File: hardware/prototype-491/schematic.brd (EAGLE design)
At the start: 160 x 100 mm, 22 parts, among them IC1 LM2576T, IC2 LM2576T, Q1 220mA/50V/3.5Ω, Q2 220mA/50V/3.5Ω

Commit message: routed signals
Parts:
- added J2: (no value), SparkFun-Connectors:MOLEX-1X2
- moved J1 189.3 mm to (83.8, 96.5), turned to 180 degrees
- moved Q1 179.0 mm to (97.8, 12.7), turned to 270 degrees
- moved C4 161.8 mm to (92.7, 36.8), turned to 270 degrees
- moved R5 157.7 mm to (105.4, 40.6), turned to 270 degrees
- moved R4 151.0 mm to (105.4, 29.2), turned to 270 degrees
- moved C2 146.2 mm to (92.7, 54.6), turned to 180 degrees
- moved R3 145.1 mm to (105.4, 19.1), turned to 270 degrees
- moved JP8 144.6 mm to (67.3, 67.3)
- moved R2 140.4 mm to (105.4, 8.89), turned to 270 degrees
- moved IC2 134.7 mm to (77.5, 45.7), turned to 180 degrees
- moved MCU 131.7 mm to (5.08, 102.9), turned to 270 degrees
- moved D2 129.3 mm to (72.4, 7.62), turned to 180 degrees
- moved IC1 123.3 mm to (77.5, 16.5), turned to 180 degrees
- moved Q2 121.5 mm to (97.8, 25.4), turned to 90 degrees
- moved R1 112.5 mm to (36.8, 27.9), turned to 270 degrees
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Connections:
- net GND: now also J2.2
- net VCC: now also J2.1
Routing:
- net +5V: track 0.00 -> 220.4 mm
- net TX_3V3: track 0.00 -> 111.7 mm, vias 0 -> 1
- net 3.3V: track 0.00 -> 107.7 mm
- net TX_5V: track 0.00 -> 92.9 mm
- net RX_5V: track 0.00 -> 69.5 mm
- net SDA: track 0.00 -> 67.9 mm
- net SCL: track 0.00 -> 61.8 mm
- net N$4: track 0.00 -> 39.5 mm
- net N$1: track 0.00 -> 34.6 mm
- net VCC: track 0.00 -> 26.9 mm
- net N$9: track 0.00 -> 13.7 mm
- net RX_3V3: track 0.00 -> 10.0 mm
- added copper zone on layer 1, net GND
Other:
- board size 160 x 100 mm -> 116.8 x 110.2 mm
- board text added: "ADXL345 Board"
- board text added: "GND"
- board text added: "VS"

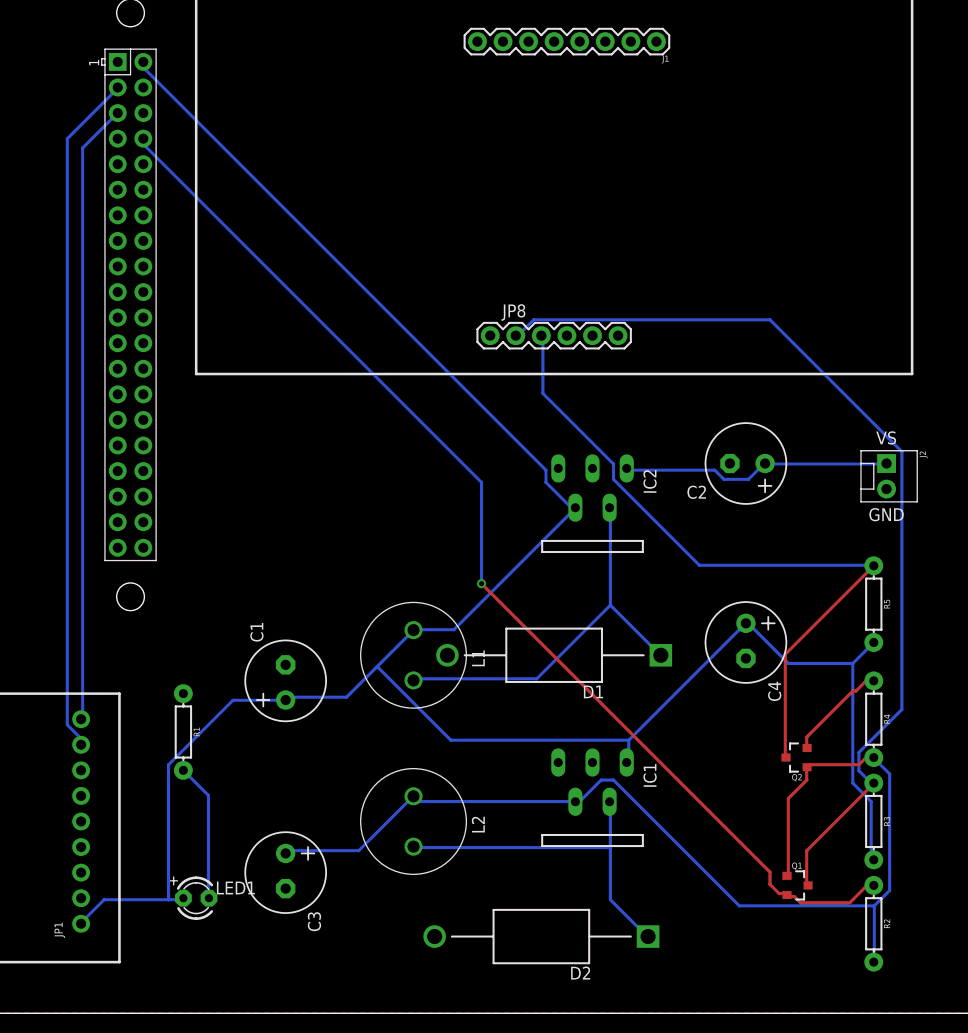
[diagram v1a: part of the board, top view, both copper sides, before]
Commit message: added status LEDs to main board, completed board for CAN test module
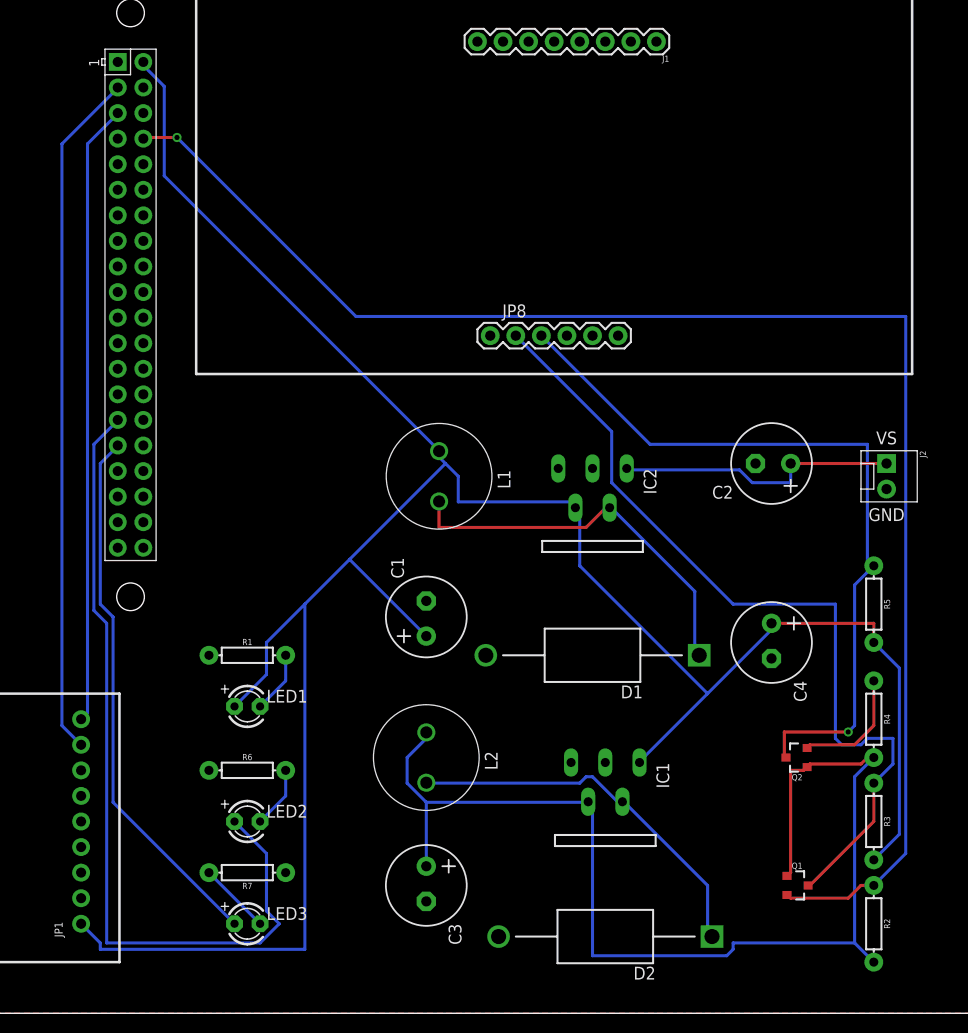
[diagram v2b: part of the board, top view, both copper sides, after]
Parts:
- added LED2, LED3: (no value), adafruit:LED3MM
- added R6, R7: 10k, SparkFun-Resistors:AXIAL-0.3
- moved LED1 19.7 mm to (43.2, 30.5)
- moved L1 18.0 mm to (62.2, 53.3)
- moved C1 15.3 mm to (61.0, 39.4)
- moved C3 14.0 mm to (61.0, 12.7)
- moved R1 9.92 mm to (43.2, 35.6), turned to 0 degrees
- moved L2 6.48 mm to (61.0, 25.4)
- moved D2 6.35 mm to (78.7, 7.62)
- moved D1 3.81 mm to (77.5, 35.6)
- moved C2 2.54 mm to (95.2, 54.6)
- moved C4 2.54 mm to (95.2, 36.8)
- moved IC1 1.27 mm to (78.7, 16.5)
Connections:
- new net N$2: LED2.A, MCU.29
- new net N$3: LED3.A, MCU.31
- new net N$5: LED2.K, R6.P$2
- new net N$6: LED3.K, R7.P$2
- net GND: now also R6.P$1, R7.P$1
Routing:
- net N$2: track 0.00 -> 83.4 mm
- net N$3: track 0.00 -> 53.7 mm
- net TX_3V3: track 111.7 -> 150.2 mm
- net +5V: track 220.4 -> 249.3 mm
- net TX_5V: track 92.9 -> 83.5 mm
- net N$9: track 13.7 -> 6.13 mm
- net N$6: track 0.00 -> 7.18 mm
- net 3.3V: track 107.7 -> 114.9 mm
- net RX_5V: track 69.5 -> 76.2 mm, vias 0 -> 1
- net N$5: track 0.00 -> 6.13 mm
- net N$1: track 34.6 -> 38.2 mm
- net RX_3V3: track 10.0 -> 12.0 mm
- net VCC: track 26.9 -> 28.3 mm

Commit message: CAM files for PCB
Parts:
- J1: value (none) -> OBD_CONN
- J2: value (none) -> SUPPLY
- JP1: value (none) -> ADXL345
- JP8: value DNP -> UART_CONN
- L1, L2: value (none) -> 100uH
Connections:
- removed net VCC: C2.+, IC2.1, J2.1
- net VBAT: now also C2.+, IC2.1, J2.1
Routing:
- net VBAT: track 0.00 -> 79.8 mm, vias 0 -> 1
- net TX_3V3: track 150.2 -> 116.0 mm
- net N$2: track 83.4 -> 49.9 mm
- net VCC: track 28.3 -> 0.00 mm
- net +5V: track 249.3 -> 234.0 mm, vias 0 -> 1
- net TX_5V: track 83.5 -> 93.2 mm
- net RX_5V: track 76.2 -> 69.7 mm, vias 1 -> 0
- net 3.3V: track 114.9 -> 108.7 mm
- net N$4: track 39.0 -> 36.5 mm
- net RX_3V3: track 12.0 -> 9.82 mm
- net N$3: track 53.7 -> 53.8 mm, vias 0 -> 1
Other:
- board text added: "ECE491Group7 Vehicle Immobilizer"

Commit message: all arduino / tester code
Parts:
- moved C1 41.2 mm to (95.2, 16.5), turned to 270 degrees
- moved Q1 5.08 mm to (97.8, 7.62)
- moved L1 4.58 mm to (59.7, 49.5), turned to 270 degrees
- moved L2 3.81 mm to (61.0, 29.2), turned to 270 degrees
- moved D1 2.54 mm to (77.5, 38.1)
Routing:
- net 3.3V: track 108.7 -> 126.9 mm, vias 0 -> 1
- net TX_5V: track 93.2 -> 79.8 mm
- net TX_3V3: track 116.0 -> 128.5 mm
- net N$1: track 38.2 -> 42.0 mm
- net +5V: track 234.0 -> 231.4 mm, vias 1 -> 0
- net VBAT: track 79.8 -> 81.4 mm, vias 1 -> 0
- net N$3: track 53.8 -> 54.5 mm
- net N$4: track 36.5 -> 37.1 mm

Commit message: test module updates
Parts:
- moved R2 74.0 mm to (44.5, 50.8), turned to 90 degrees
- moved R3 63.9 mm to (44.5, 38.1), turned to 90 degrees
- moved R5 55.5 mm to (50.8, 50.8), turned to 90 degrees
- moved R4 55.3 mm to (50.8, 38.1), turned to 90 degrees
- moved Q1 53.8 mm to (47.0, 25.4), turned to 0 degrees
- moved Q2 51.8 mm to (47.0, 15.2), turned to 0 degrees
- moved C3 44.7 mm to (97.8, 38.1), turned to 90 degrees
- moved L1 44.0 mm to (96.5, 25.4), turned to 0 degrees
- moved L2 40.3 mm to (96.5, 10.2), turned to 0 degrees
- moved C1 17.3 mm to (78.7, 21.6)
- moved R1 16.1 mm to (38.1, 50.8), turned to 270 degrees
- moved R6 14.9 mm to (38.1, 38.1), turned to 270 degrees
- moved D2 14.5 mm to (64.8, 11.4)
- moved IC1 13.3 mm to (66.0, 20.3)
- moved D1 11.4 mm to (66.0, 38.1)
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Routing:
- net TX_3V3: track 128.5 -> 64.1 mm, vias 1 -> 0
- net +5V: track 231.4 -> 192.0 mm
- net TX_5V: track 79.8 -> 57.6 mm
- net 3.3V: track 126.9 -> 148.0 mm, vias 1 -> 4
- net N$9: track 6.19 -> 23.4 mm, vias 0 -> 1
- net RX_3V3: track 9.81 -> 21.2 mm, vias 0 -> 1
- net N$5: track 6.12 -> 17.5 mm, vias 0 -> 1
- net N$2: track 49.7 -> 39.1 mm, vias 0 -> 1
- net N$4: track 37.1 -> 47.3 mm
- net VBAT: track 81.4 -> 71.3 mm
- net N$3: track 54.5 -> 45.3 mm
- net RX_5V: track 70.1 -> 61.1 mm, vias 0 -> 1
- net N$1: track 42.0 -> 35.9 mm
- net SCL: track 61.8 -> 59.0 mm
- net SDA: track 68.0 -> 65.4 mm
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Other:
- board size 116.8 x 110.2 mm -> 111.7 x 103.8 mm

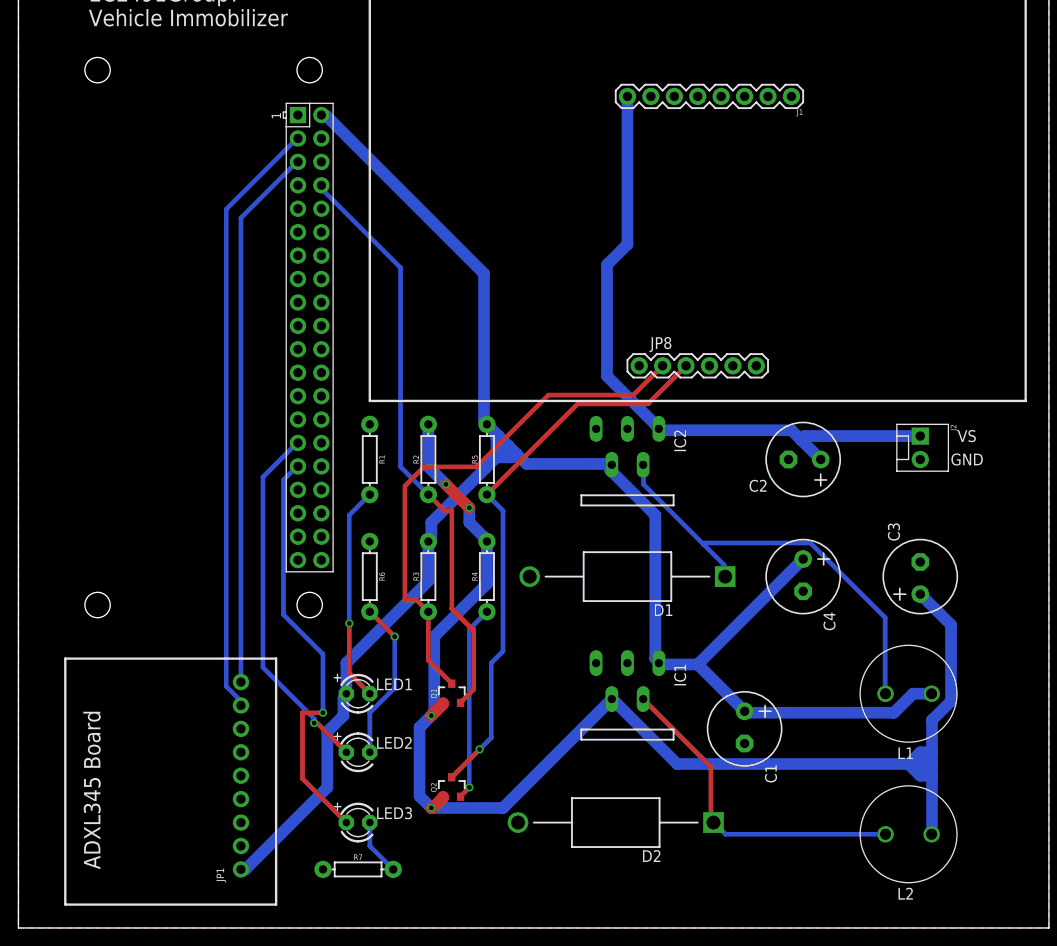
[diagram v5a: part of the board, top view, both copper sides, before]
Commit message: android app plus updated board
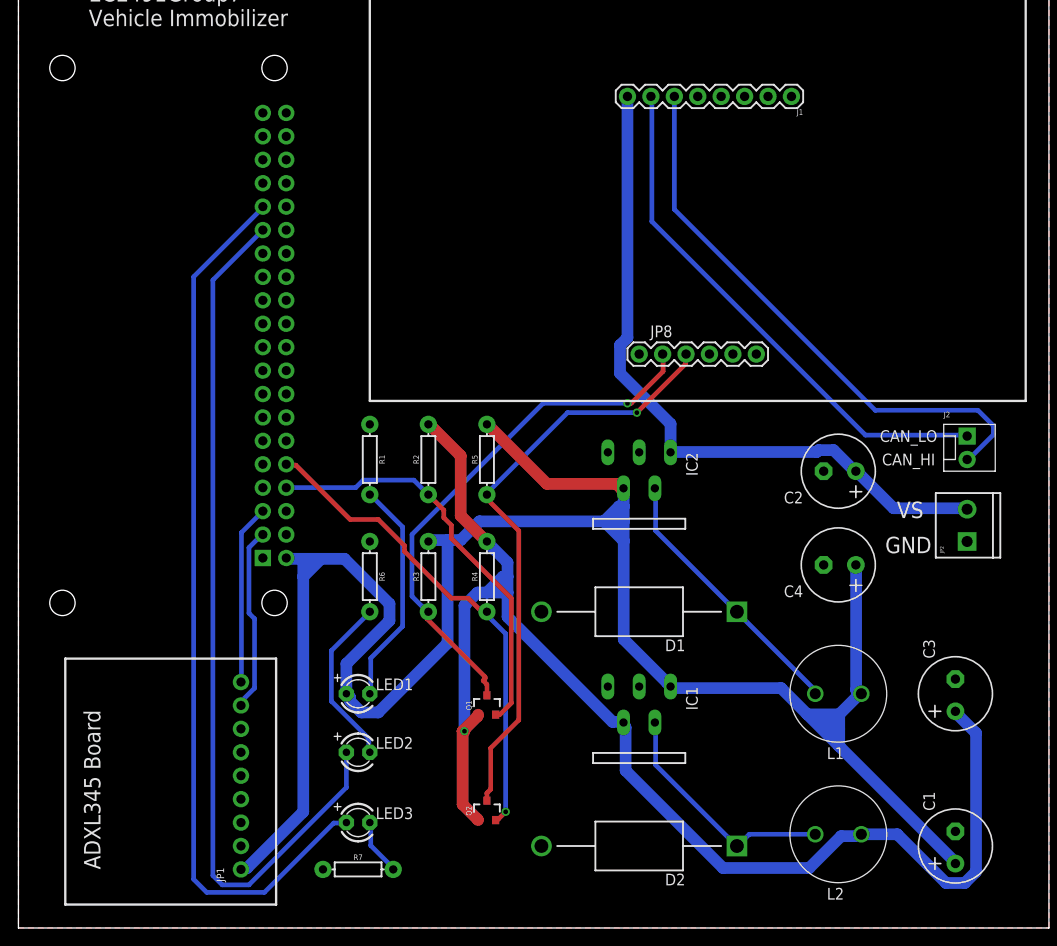
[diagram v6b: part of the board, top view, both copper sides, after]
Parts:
- added JP2: SUPPLY, SparkFun:SCREWTERMINAL-3.5MM-2
- J2: value SUPPLY -> CAN
- R1, R6, R7: value 10k -> 330
- moved MCU 64.9 mm to (1.27, 31.8), flipped to the bottom, turned to 90 degrees
- moved C1 26.2 mm to (101.6, 8.89), turned to 90 degrees
- moved C3 13.3 mm to (101.6, 25.4)
- moved L1 7.62 mm to (88.9, 25.4)
- moved L2 7.62 mm to (88.9, 10.2)
- moved J2 5.08 mm to (102.9, 53.3)
- moved Q2 4.58 mm to (50.8, 12.7)
- moved C2 4.02 mm to (88.9, 49.5)
- moved C4 4.02 mm to (88.9, 39.4), turned to 180 degrees
- moved D1 4.02 mm to (67.3, 34.3)
- moved Q1 4.02 mm to (50.8, 24.1)
- moved D2 3.59 mm to (67.3, 8.89)
- moved IC1 2.84 mm to (67.3, 17.8)
- moved IC2 2.84 mm to (67.3, 43.2)
- moved JP8 1.27 mm to (67.3, 62.2)
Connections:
- net N$2 renamed STAT_LED1
- net N$3 renamed STAT_LED2
- removed net RX3V3: MCU.10
- net CAN_HI: now also J2.2
- net CAN_LO: now also J2.1
- net GND: now also JP2.1, MCU.14, MCU.20, MCU.25, MCU.30, MCU.39, MCU.6, MCU.9; no longer J2.2
- net RX_3V3: now also MCU.10
- net VBAT: now also JP2.2; no longer J2.1
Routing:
- net CAN_HI: track 0.00 -> 61.5 mm
- net CAN_LO: track 0.00 -> 57.4 mm
- net STAT_LED1: track 39.1 -> 95.3 mm, vias 1 -> 0
- net STAT_LED2: track 45.3 -> 96.3 mm, vias 1 -> 0
- net SDA: track 65.4 -> 20.1 mm
- net SCL: track 59.0 -> 19.5 mm
- net +5V: track 192.0 -> 228.8 mm
- net RX_3V3: track 21.2 -> 52.8 mm
- net TX_3V3: track 64.1 -> 44.9 mm
- net N$4: track 47.3 -> 29.5 mm
- net N$1: track 35.9 -> 26.1 mm
- net VBAT: track 71.3 -> 76.1 mm
- net RX_5V: track 61.1 -> 64.6 mm
- net N$5: track 17.5 -> 18.7 mm, vias 1 -> 0
- net N$9: track 23.4 -> 24.6 mm, vias 1 -> 0
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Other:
- board text added: "CAN_HI"
- board text added: "CAN_LO"
